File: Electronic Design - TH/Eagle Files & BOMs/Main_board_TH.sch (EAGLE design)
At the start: 43 parts, among them M1 ARDUINO-NANO-3.0, Q1 IRF9520, Q2 IRF9520

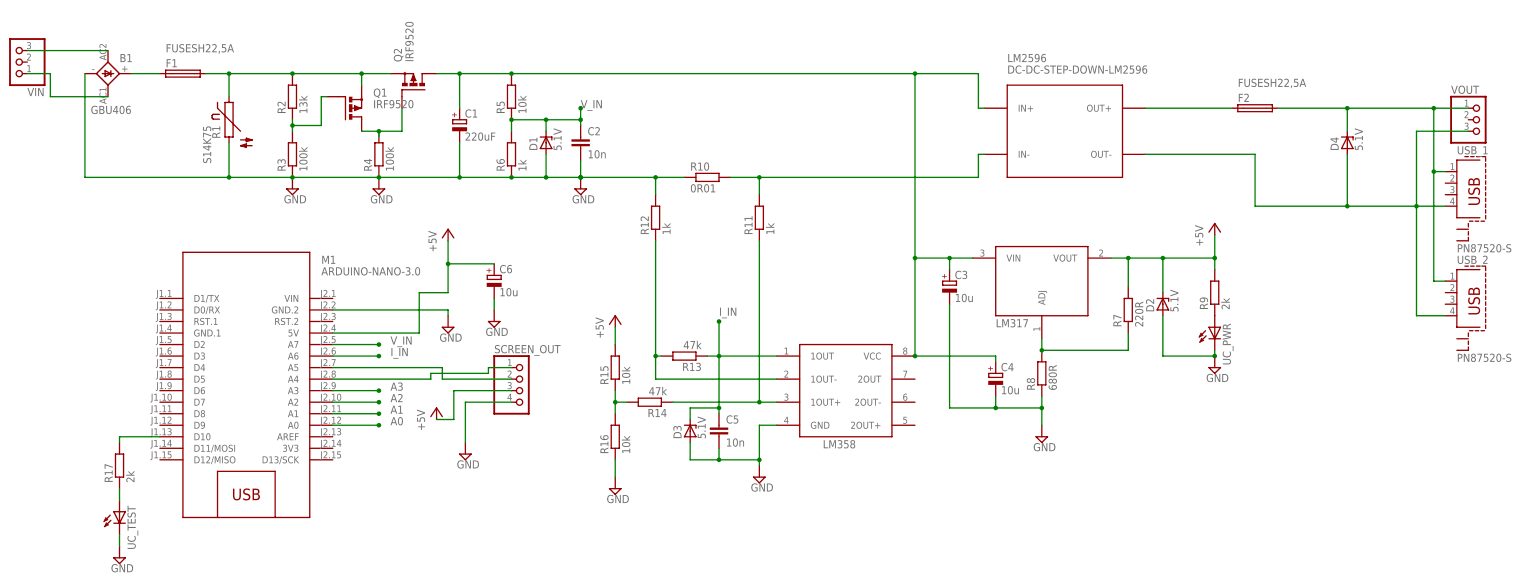
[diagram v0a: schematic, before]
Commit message: adding in test points and jumpers
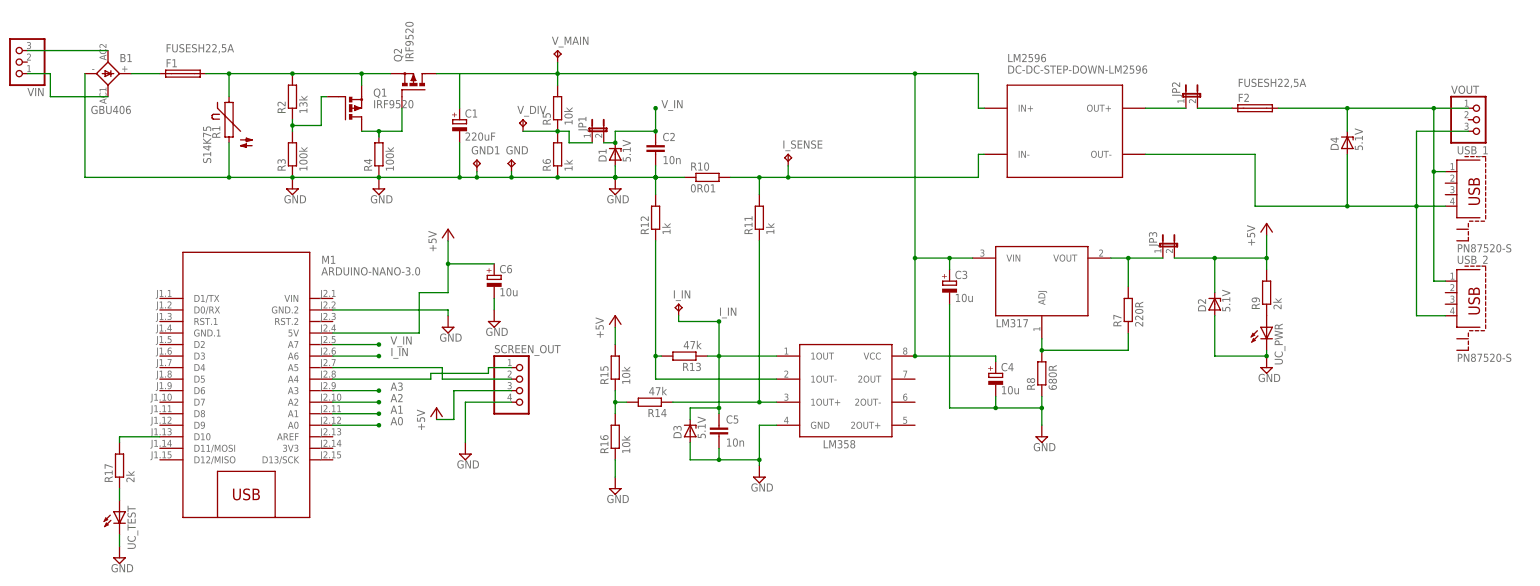
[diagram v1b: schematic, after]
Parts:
- added GND, GND1, I_IN, I_SENSE, V_DIV, V_MAIN: TPPAD1-13, testpad:TPPAD1-13
- added JP1, JP2, JP3: (no value), jumper:JP1E
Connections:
- removed net VOUT_PREFUSE: F2.1, LM2596.OUT+
- new net N$15: JP2.1, LM2596.OUT+
- new net N$16: F2.1, JP2.2
- new net N$17: JP1.1, R5.1, R6.2, V_DIV.TP
- new net N$18: JP3.1, LM317.VOUT, R7.2
- net +5V: now also JP3.2; no longer LM317.VOUT, R7.2
- net GND: now also GND.TP, GND1.TP
- net I_IN: now also I_IN.TP
- net N$4: now also I_SENSE.TP
- net VIN_PROTECTED: now also V_MAIN.TP
- net V_IN: now also JP1.2; no longer R5.1, R6.2
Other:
- moved on the sheet: C2, D1, D2, R5, R6, R9, UC_PWR

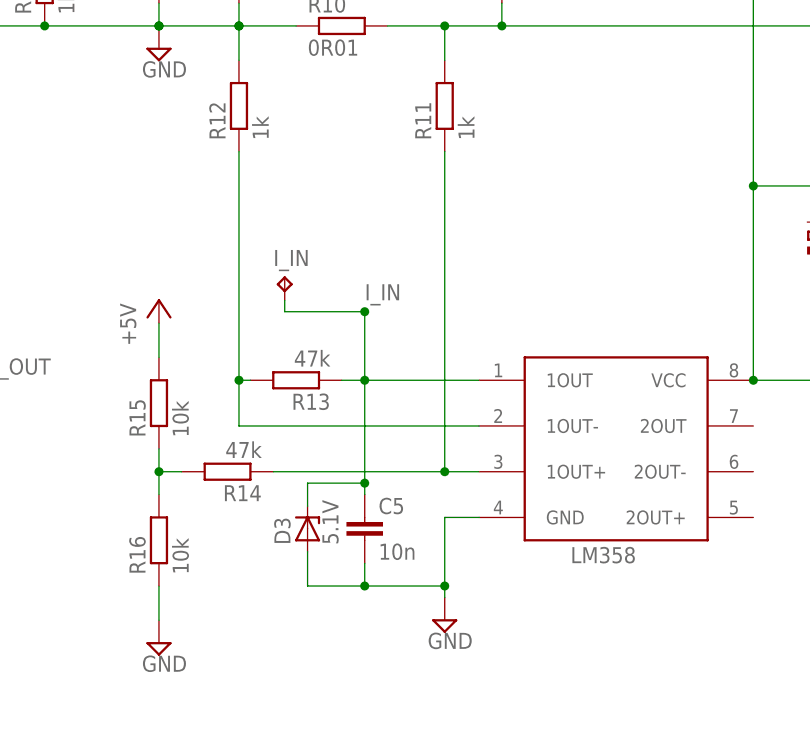
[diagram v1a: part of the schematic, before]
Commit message: adding another jumper after current sensing and more routing done
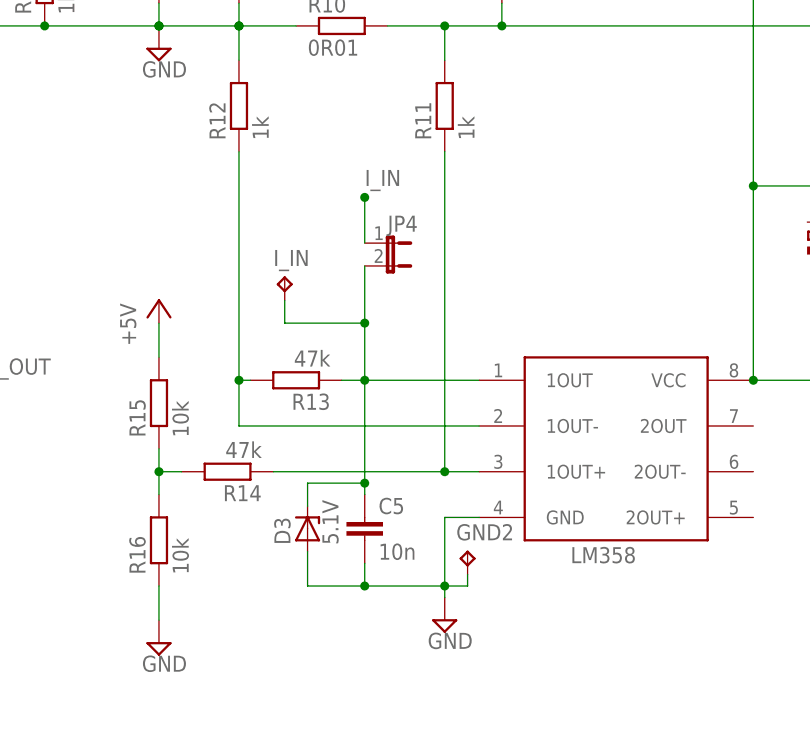
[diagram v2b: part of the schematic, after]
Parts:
- added GND2: TPPAD1-13, testpad:TPPAD1-13
- added JP4: (no value), jumper:JP1E
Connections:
- net GND: now also GND2.TP
- net I_IN: now also JP4.1, JP4.2
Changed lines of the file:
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@@
 <part name="JP2" library="jumper" deviceset="JP1E" device=""/>
 <part name="JP3" library="jumper" deviceset="JP1E" device=""/>
+<part name="GND2" library="testpad" deviceset="TP" device="PAD1-13" value="TPPAD1-13"/>
+<part name="JP4" library="jumper" deviceset="JP1E" device=""/>
 </parts>
 <sheets>
@@
 <instance part="JP2" gate="A" x="128.27" y="83.82"/>
 <instance part="JP3" gate="A" x="123.19" y="50.8"/>
+<instance part="GND2" gate="G$1" x="36.83" y="7.62"/>
+<instance part="JP4" gate="A" x="27.94" y="41.91" rot="R270"/>
 </instances>
 <busses>
@@
 <wire x1="19.05" y1="3.81" x2="25.4" y2="3.81" width="0.1524" layer="91"/>
 <junction x="25.4" y="3.81"/>
+<pinref part="GND2" gate="G$1" pin="TP"/>
+<wire x1="34.29" y1="3.81" x2="36.83" y2="3.81" width="0.1524" layer="91"/>
+<wire x1="36.83" y1="3.81" x2="36.83" y2="5.08" width="0.1524" layer="91"/>
 </segment>
 <segment>
@@
 <wire x1="22.86" y1="26.67" x2="25.4" y2="26.67" width="0.1524" layer="91"/>
 <wire x1="25.4" y1="26.67" x2="38.1" y2="26.67" width="0.1524" layer="91"/>
-<wire x1="25.4" y1="26.67" x2="25.4" y2="34.29" width="0.1524" layer="91"/>
-<junction x="25.4" y="34.29"/>
-<label x="25.4" y="35.56" size="1.778" layer="95"/>
 <junction x="25.4" y="26.67"/>
 <pinref part="C5" gate="G$1" pin="1"/>
@@
 <wire x1="19.05" y1="15.24" x2="19.05" y2="12.7" width="0.1524" layer="91"/>
 <junction x="25.4" y="15.24"/>
+<pinref part="JP4" gate="A" pin="2"/>
+<wire x1="25.4" y1="39.37" x2="25.4" y2="33.02" width="0.1524" layer="91"/>
 <pinref part="I_IN" gate="G$1" pin="TP"/>
-<wire x1="16.51" y1="35.56" x2="16.51" y2="34.29" width="0.1524" layer="91"/>
-<wire x1="16.51" y1="34.29" x2="25.4" y2="34.29" width="0.1524" layer="91"/>
+<wire x1="25.4" y1="33.02" x2="25.4" y2="26.67" width="0.1524" layer="91"/>
+<wire x1="16.51" y1="35.56" x2="16.51" y2="33.02" width="0.1524" layer="91"/>
+<wire x1="16.51" y1="33.02" x2="25.4" y2="33.02" width="0.1524" layer="91"/>
+<junction x="25.4" y="33.02"/>
 </segment>
 <segment>
@@
 <label x="-46.99" y="26.67" size="1.778" layer="95"/>
 </segment>
-</net>
+<segment>
+<pinref part="JP4" gate="A" pin="1"/>
+<wire x1="25.4" y1="41.91" x2="25.4" y2="46.99" width="0.1524" layer="91"/>
+<junction x="25.4" y="46.99"/>
+<label x="25.4" y="48.26" size="1.778" layer="95"/>
+</segment>
+</net>

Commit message: finishing routing
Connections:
- new net I_IN_PRE: I_IN.TP, JP4.2, LM358.1OUT, R13.1
- net GND: now also M1.GND.1
- net I_IN: no longer I_IN.TP, JP4.2, LM358.1OUT, R13.1
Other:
- moved on the sheet: C5, D3, GND2, I_IN, JP4, R15, R16, SCREEN_OUT

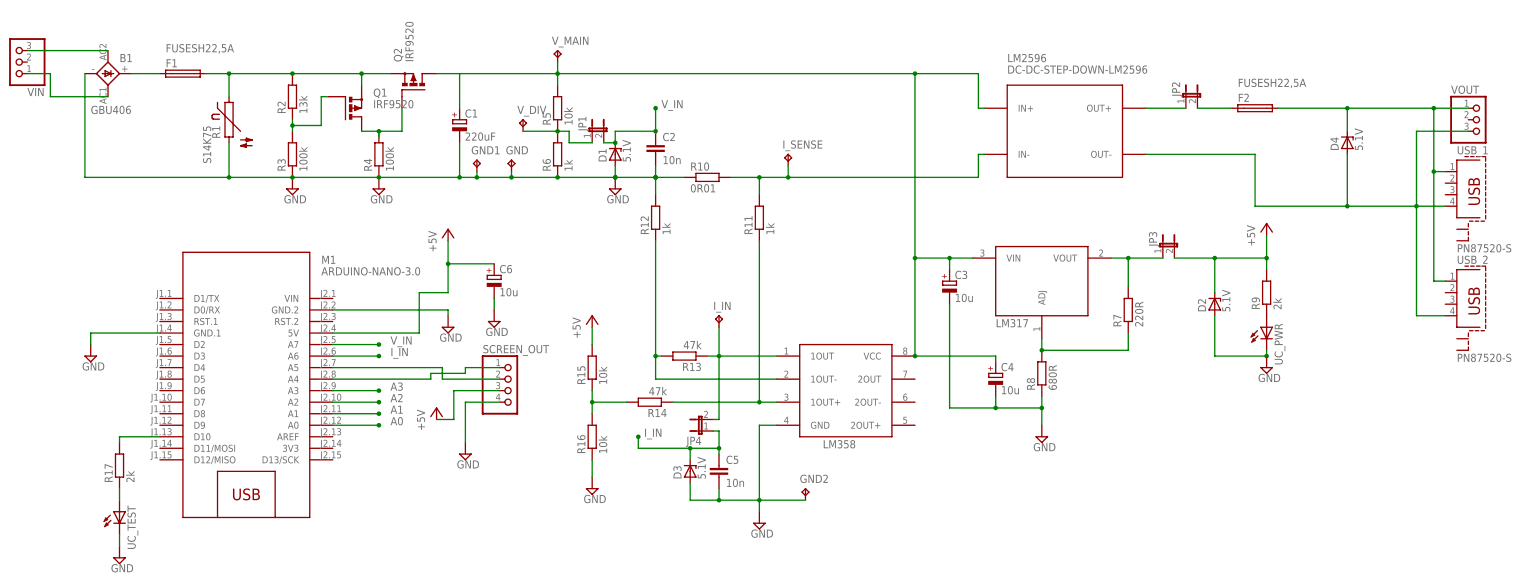
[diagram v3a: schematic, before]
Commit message: adding in numbers for items on block diagramme
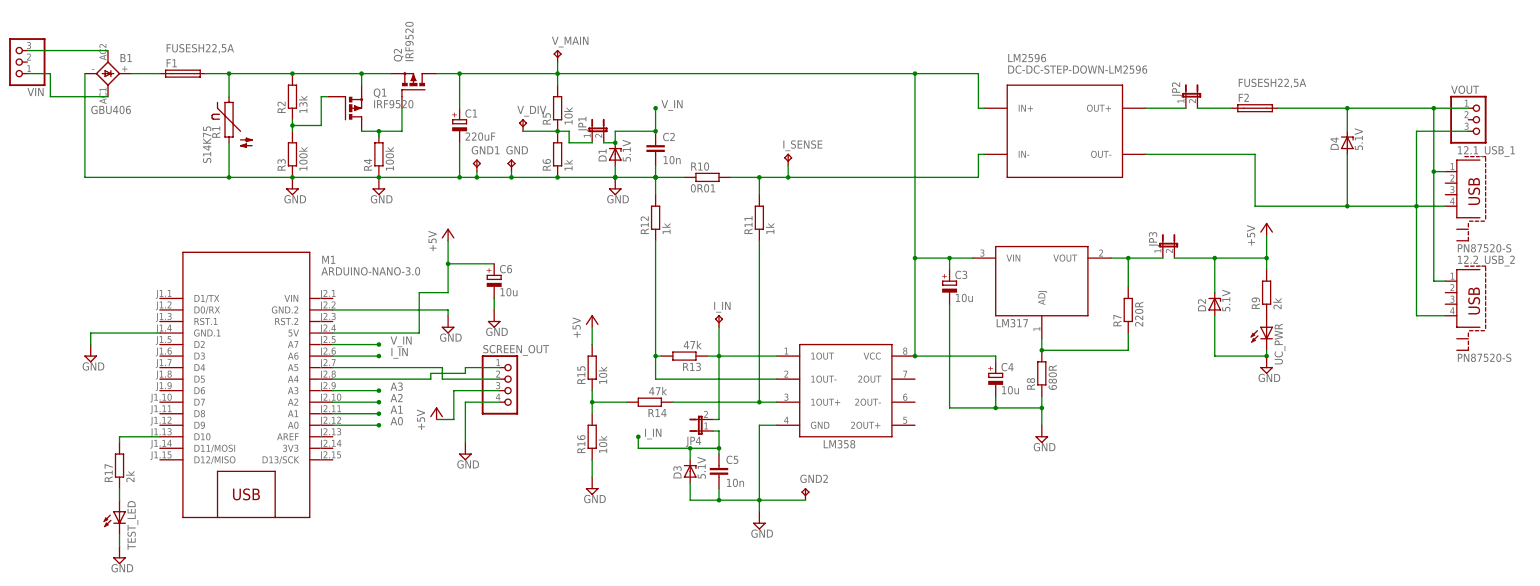
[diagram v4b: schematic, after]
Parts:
- renumbered UC_TEST to TEST_LED, USB_1 to 12.1_USB_1, USB_2 to 12.2_USB_2
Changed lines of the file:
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@@
 <part name="R2" library="resistor" deviceset="R-EU_" device="0207/10" value="13k"/>
 <part name="R3" library="resistor" deviceset="R-EU_" device="0207/10" value="100k"/>
-<part name="USB_1" library="con-berg" deviceset="PN87520-S" device=""/>
-<part name="USB_2" library="con-berg" deviceset="PN87520-S" device=""/>
-<part name="UC_TEST" library="led" deviceset="LED" device="3MM"/>
+<part name="12.1_USB_1" library="con-berg" deviceset="PN87520-S" device=""/>
+<part name="12.2_USB_2" library="con-berg" deviceset="PN87520-S" device=""/>
+<part name="TEST_LED" library="led" deviceset="LED" device="3MM"/>
 <part name="R17" library="resistor" deviceset="R-EU_" device="0207/10" value="2k"/>
 <part name="SUPPLY2" library="supply2" deviceset="GND" device=""/>
@@
 <instance part="R2" gate="G$1" x="-68.58" y="83.82" rot="R90"/>
 <instance part="R3" gate="G$1" x="-68.58" y="71.12" rot="R90"/>
-<instance part="USB_1" gate="G$1" x="187.96" y="62.23"/>
-<instance part="USB_2" gate="G$1" x="187.96" y="38.1"/>
-<instance part="UC_TEST" gate="G$1" x="-106.68" y="-7.62" smashed="yes">
+<instance part="12.1_USB_1" gate="G$1" x="187.96" y="62.23"/>
+<instance part="12.2_USB_2" gate="G$1" x="187.96" y="38.1"/>
+<instance part="TEST_LED" gate="G$1" x="-106.68" y="-7.62" smashed="yes">
 <attribute name="NAME" x="-103.124" y="-16.002" size="1.778" layer="95" rot="R90"/>
 <attribute name="VALUE" x="-100.965" y="-12.192" size="1.778" layer="96" rot="R90"/>
@@
 </segment>
 <segment>
-<pinref part="UC_TEST" gate="G$1" pin="C"/>
+<pinref part="TEST_LED" gate="G$1" pin="C"/>
 <pinref part="SUPPLY2" gate="GND" pin="GND"/>
 <wire x1="-106.68" y1="-12.7" x2="-106.68" y2="-15.24" width="0.1524" layer="91"/>
@@
 <wire x1="-10.16" y1="88.9" x2="-10.16" y2="91.44" width="0.1524" layer="91"/>
 <junction x="68.58" y="88.9"/>
+<junction x="-31.75" y="88.9"/>
 </segment>
 </net>
@@
 <wire x1="182.88" y1="81.28" x2="190.5" y2="81.28" width="0.1524" layer="91"/>
 <wire x1="182.88" y1="81.28" x2="182.88" y2="67.31" width="0.1524" layer="91"/>
-<pinref part="USB_1" gate="G$1" pin="1"/>
+<pinref part="12.1_USB_1" gate="G$1" pin="1"/>
 <wire x1="182.88" y1="67.31" x2="185.42" y2="67.31" width="0.1524" layer="91"/>
 <wire x1="182.88" y1="67.31" x2="182.88" y2="43.18" width="0.1524" layer="91"/>
-<pinref part="USB_2" gate="G$1" pin="1"/>
+<pinref part="12.2_USB_2" gate="G$1" pin="1"/>
 <wire x1="182.88" y1="43.18" x2="185.42" y2="43.18" width="0.1524" layer="91"/>
 <junction x="182.88" y="67.31"/>
@@
 <wire x1="143.51" y1="71.12" x2="143.51" y2="59.69" width="0.1524" layer="91"/>
 <wire x1="143.51" y1="59.69" x2="163.83" y2="59.69" width="0.1524" layer="91"/>
-<pinref part="USB_1" gate="G$1" pin="4"/>
+<pinref part="12.1_USB_1" gate="G$1" pin="4"/>
 <wire x1="185.42" y1="59.69" x2="179.07" y2="59.69" width="0.1524" layer="91"/>
 <wire x1="179.07" y1="59.69" x2="179.07" y2="35.56" width="0.1524" layer="91"/>
-<pinref part="USB_2" gate="G$1" pin="4"/>
+<pinref part="12.2_USB_2" gate="G$1" pin="4"/>
 <wire x1="179.07" y1="35.56" x2="185.42" y2="35.56" width="0.1524" layer="91"/>
 <junction x="179.07" y="59.69"/>
@@
 <segment>
 <pinref part="R17" gate="G$1" pin="1"/>
-<pinref part="UC_TEST" gate="G$1" pin="A"/>
+<pinref part="TEST_LED" gate="G$1" pin="A"/>
 <wire x1="-106.68" y1="-2.54" x2="-106.68" y2="-5.08" width="0.1524" layer="91"/>
 </segment>

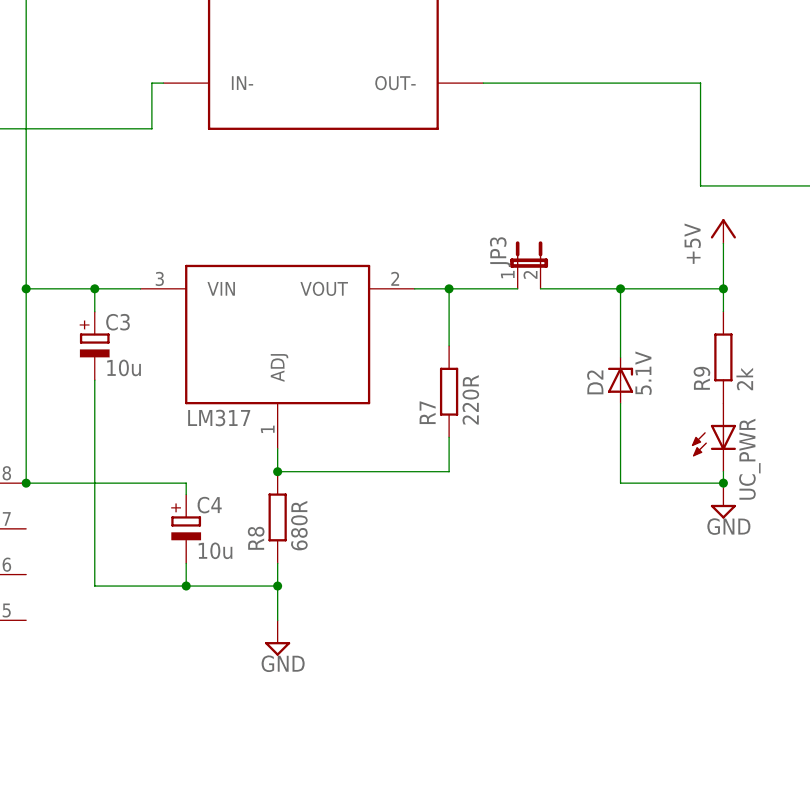
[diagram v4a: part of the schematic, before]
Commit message: adding test points for LM317
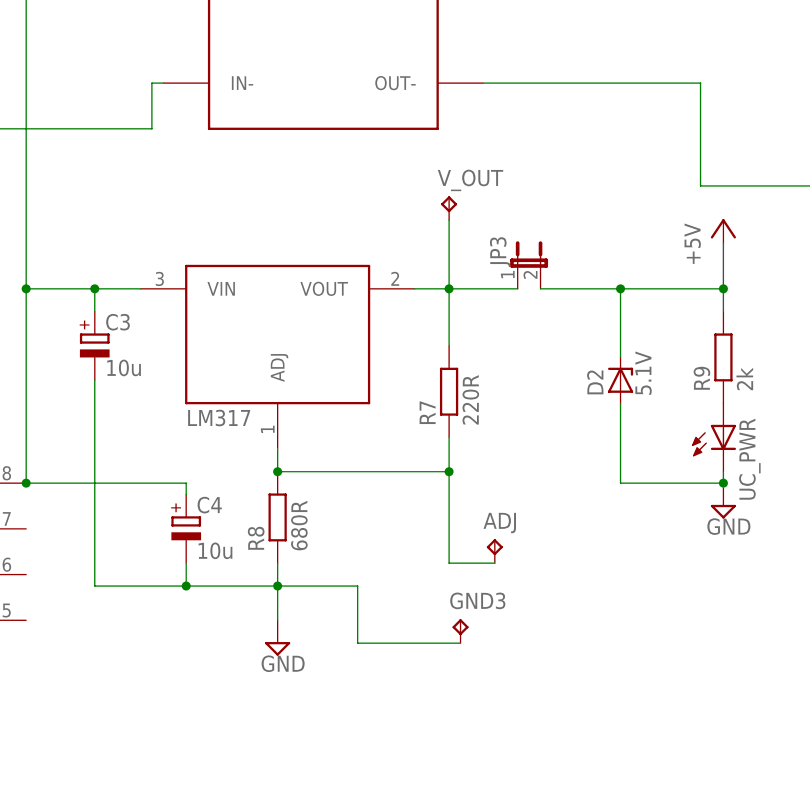
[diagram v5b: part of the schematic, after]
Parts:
- added ADJ, GND3, V_OUT: TPPAD1-13, testpad:TPPAD1-13
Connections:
- net GND: now also GND3.TP
- net N$18: now also V_OUT.TP
- net N$23: now also ADJ.TP
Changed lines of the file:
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@@
 <part name="JP4" library="jumper" deviceset="JP1E" device=""/>
 <part name="SUPPLY3" library="supply2" deviceset="GND" device=""/>
+<part name="V_OUT" library="testpad" deviceset="TP" device="PAD1-13" value="TPPAD1-13"/>
+<part name="ADJ" library="testpad" deviceset="TP" device="PAD1-13" value="TPPAD1-13"/>
+<part name="GND3" library="testpad" deviceset="TP" device="PAD1-13" value="TPPAD1-13"/>
 </parts>
 <sheets>
@@
 <instance part="JP4" gate="A" x="21.59" y="10.16" rot="R90"/>
 <instance part="SUPPLY3" gate="GND" x="-113.03" y="26.67"/>
+<instance part="V_OUT" gate="G$1" x="115.57" y="58.42"/>
+<instance part="ADJ" gate="G$1" x="120.65" y="20.32"/>
+<instance part="GND3" gate="G$1" x="116.84" y="11.43"/>
 </instances>
 <busses>
@@
 <wire x1="76.2" y1="15.24" x2="86.36" y2="15.24" width="0.1524" layer="91"/>
 <junction x="86.36" y="15.24"/>
+<pinref part="GND3" gate="G$1" pin="TP"/>
+<wire x1="116.84" y1="8.89" x2="105.41" y2="8.89" width="0.1524" layer="91"/>
+<wire x1="105.41" y1="8.89" x2="105.41" y2="15.24" width="0.1524" layer="91"/>
+<wire x1="105.41" y1="15.24" x2="96.52" y2="15.24" width="0.1524" layer="91"/>
 </segment>
 <segment>
@@
 <junction x="96.52" y="27.94"/>
 <pinref part="LM317" gate="G$1" pin="ADJ"/>
+<wire x1="115.57" y1="27.94" x2="115.57" y2="17.78" width="0.1524" layer="91"/>
+<pinref part="ADJ" gate="G$1" pin="TP"/>
+<wire x1="115.57" y1="17.78" x2="120.65" y2="17.78" width="0.1524" layer="91"/>
+<junction x="115.57" y="27.94"/>
 </segment>
 </net>
@@
 <wire x1="115.57" y1="48.26" x2="123.19" y2="48.26" width="0.1524" layer="91"/>
 <junction x="115.57" y="48.26"/>
-</segment>
-</net>
+<pinref part="V_OUT" gate="G$1" pin="TP"/>
+<wire x1="115.57" y1="55.88" x2="115.57" y2="48.26" width="0.1524" layer="91"/>
+</segment>
+</net>
